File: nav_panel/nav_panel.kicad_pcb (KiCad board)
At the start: 2 copper layers, 45.7 x 22.6 mm, 12 parts, among them J1 Conn_01x04_Male, J2 Conn_01x04_Male, SW1 SW_Push, SW2 SW_Push

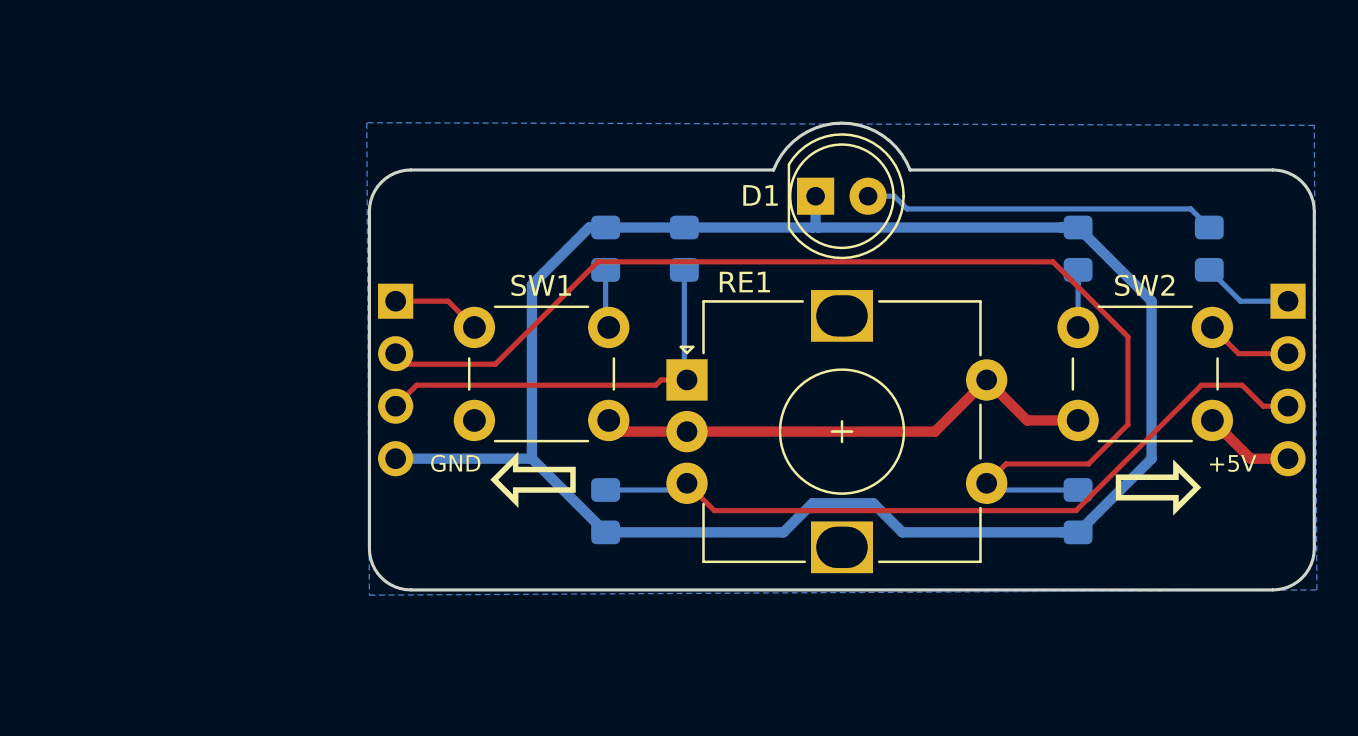
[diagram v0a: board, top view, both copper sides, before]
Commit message: Wide nav_panel version.
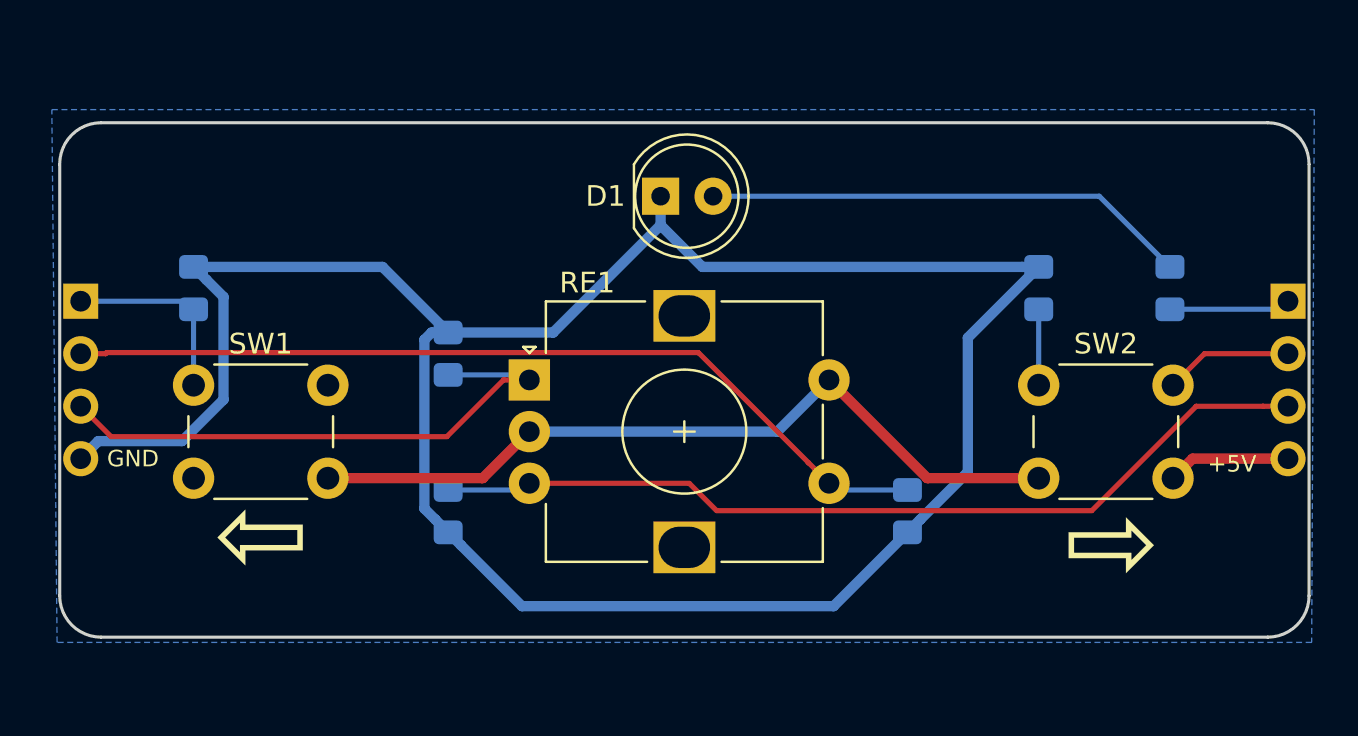
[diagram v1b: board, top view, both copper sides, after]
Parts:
- moved R1 20.0 mm to (117.2, 85.7)
- moved J1 15.2 mm to (111.8, 86.4)
- moved SW1 13.9 mm to (117.2, 90.4)
- moved R5 12.5 mm to (129.5, 88.9)
- moved R4 8.26 mm to (151.8, 96.5)
- moved RE1 7.63 mm to (133.5, 90.2)
- moved R3 7.62 mm to (129.5, 96.5)
- moved D1 7.50 mm to (139.8, 81.3)
- moved SW2 3.38 mm to (158.1, 90.4)
- moved R2 2.69 mm to (158.1, 85.7)
- moved R6 2.69 mm to (164.5, 85.7)
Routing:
- net GND: track 90.8 -> 113.5 mm
- net +5V: track 29.2 -> 44.3 mm
- net RE1: track 56.0 -> 42.8 mm
- net RE_A: track 20.0 -> 27.5 mm
- net RE_B: track 36.6 -> 43.4 mm
- net Net-(D1-Pad2): track 17.1 -> 23.5 mm
- net SW2: track 6.97 -> 9.87 mm
- net SW1: track 7.18 -> 9.30 mm
- net LED: track 4.44 -> 5.88 mm
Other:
- board size 45.7 x 22.6 mm -> 60.5 x 24.9 mm

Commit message: Printed and tested layout version.
USB still on upper board.
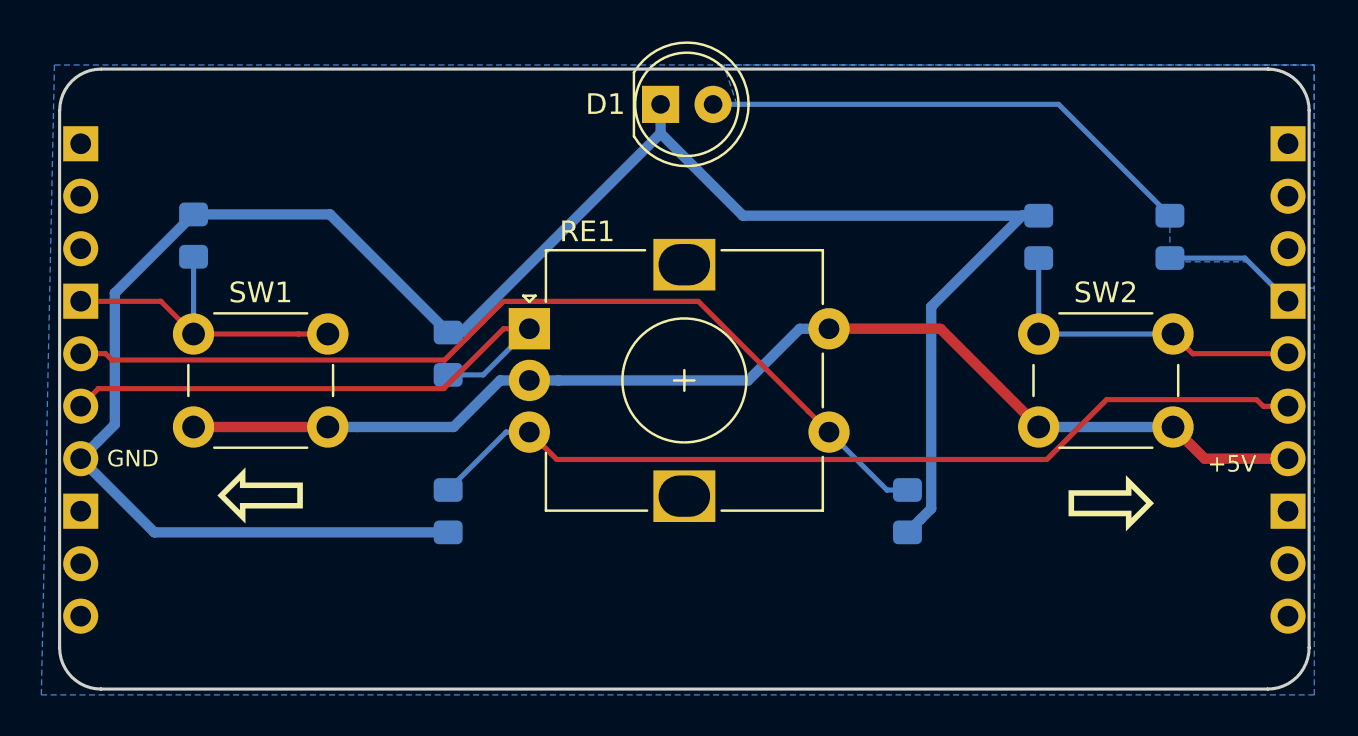
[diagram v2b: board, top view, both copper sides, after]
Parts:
- added REF**: PinHeader_1x03_P2.54mm_Vertical, Connector_PinHeader_2.54mm:PinHeader_1x03_P2.54mm_Vertical, B.Cu at (170.2, 78.7)
- added REF**: PinHeader_1x03_P2.54mm_Vertical, Connector_PinHeader_2.54mm:PinHeader_1x03_P2.54mm_Vertical, B.Cu at (170.2, 96.5)
- added REF**: PinHeader_1x03_P2.54mm_Vertical, Connector_PinHeader_2.54mm:PinHeader_1x03_P2.54mm_Vertical, B.Cu at (111.8, 96.5)
- added REF**: PinHeader_1x03_P2.54mm_Vertical, Connector_PinHeader_2.54mm:PinHeader_1x03_P2.54mm_Vertical, B.Cu at (111.8, 78.7)
- added REF**: KiCad-Logo2_5mm_SilkScreen, Symbol:KiCad-Logo2_5mm_SilkScreen, B.Cu at (130.2, 80.6)
- moved D1 4.45 mm to (139.8, 76.8)
- moved R1 2.54 mm to (117.2, 83.2)
- moved RE1 2.48 mm to (133.5, 87.7)
- moved SW1 2.48 mm to (117.2, 87.9)
- moved SW2 2.48 mm to (158.1, 87.9)
- moved R2 2.48 mm to (158.1, 83.2)
- moved R6 2.48 mm to (164.5, 83.2)
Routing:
- net +5V: track 44.3 -> 57.5 mm
- net GND: track 113.5 -> 102.1 mm
- net SW1: track 9.30 -> 16.4 mm
- net SW2: track 9.87 -> 16.1 mm
- net RE1: track 42.8 -> 45.1 mm
- net Net-(D1-Pad2): track 23.5 -> 24.3 mm
- net LED: track 5.88 -> 6.58 mm
- net RE_A: track 27.5 -> 28.1 mm
- added copper zone on B.Cu, net Net-(D1-Pad2)
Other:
- board size 60.5 x 24.9 mm -> 60.5 x 30 mm
- board text added: "2019.11.04"
- board text added: "https://github.com/mar0x/pq-4"
- board text added: "nav_panel"

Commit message: Production version 2019.11.19.
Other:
- board text added: "2019.11.18"
- board text added: "github.com/mar0x/pq-4"
- board text removed: "2019.11.04"
- board text removed: "https://github.com/mar0x/pq-4"
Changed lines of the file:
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@@
     (tags "resistor handsolder")
     (attr smd)
-    (fp_text reference R1 (at 1.397 1.778 90) (layer B.SilkS)
-      (effects (font (size 1 1) (thickness 0.15)) (justify mirror))
-    )
-    (fp_text value 10k (at -1.524 1.905 90) (layer B.SilkS)
+    (fp_text reference R1 (at 2.54 0.254 180) (layer B.SilkS)
+      (effects (font (size 1 1) (thickness 0.15)) (justify mirror))
+    )
+    (fp_text value 10k (at -2.54 0.254 180) (layer B.SilkS)
       (effects (font (size 1 1) (thickness 0.13)) (justify mirror))
     )
@@
     (tags "resistor handsolder")
     (attr smd)
-    (fp_text reference R2 (at 1.397 -1.651 90) (layer B.SilkS)
-      (effects (font (size 1 1) (thickness 0.15)) (justify mirror))
-    )
-    (fp_text value 10k (at -1.651 -1.651 90) (layer B.SilkS)
+    (fp_text reference R2 (at 2.6035 0 180) (layer B.SilkS)
+      (effects (font (size 1 1) (thickness 0.15)) (justify mirror))
+    )
+    (fp_text value 10k (at -2.4765 0 180) (layer B.SilkS)
       (effects (font (size 1 1) (thickness 0.13)) (justify mirror))
     )
@@
     (tags "resistor handsolder")
     (attr smd)
-    (fp_text reference R3 (at -1.397 1.65 270) (layer B.SilkS)
-      (effects (font (size 1 1) (thickness 0.15)) (justify mirror))
-    )
-    (fp_text value 10k (at 1.524 1.651 270) (layer B.SilkS)
+    (fp_text reference R3 (at -2.54 0) (layer B.SilkS)
+      (effects (font (size 1 1) (thickness 0.15)) (justify mirror))
+    )
+    (fp_text value 10k (at 2.54 0) (layer B.SilkS)
       (effects (font (size 1 1) (thickness 0.13)) (justify mirror))
     )
@@
     (tags "resistor handsolder")
     (attr smd)
-    (fp_text reference R4 (at -1.27 1.651 270) (layer B.SilkS)
-      (effects (font (size 1 1) (thickness 0.15)) (justify mirror))
-    )
-    (fp_text value 10k (at 1.524 1.651 270) (layer B.SilkS)
+    (fp_text reference R4 (at -2.54 0) (layer B.SilkS)
+      (effects (font (size 1 1) (thickness 0.15)) (justify mirror))
+    )
+    (fp_text value 10k (at 2.54 0) (layer B.SilkS)
       (effects (font (size 1 1) (thickness 0.13)) (justify mirror))
     )
@@
     (tags "resistor handsolder")
     (attr smd)
-    (fp_text reference R5 (at 1.397 -1.651 90) (layer B.SilkS)
-      (effects (font (size 1 1) (thickness 0.15)) (justify mirror))
-    )
-    (fp_text value 10k (at -1.524 -1.65 90) (layer B.SilkS)
+    (fp_text reference R5 (at 2.54 0 180) (layer B.SilkS)
+      (effects (font (size 1 1) (thickness 0.15)) (justify mirror))
+    )
+    (fp_text value 10k (at -2.54 0 180) (layer B.SilkS)
       (effects (font (size 1 1) (thickness 0.13)) (justify mirror))
     )
@@
     (tags "resistor handsolder")
     (attr smd)
-    (fp_text reference R6 (at -1.397 1.65 270) (layer B.SilkS)
-      (effects (font (size 1 1) (thickness 0.15)) (justify mirror))
-    )
-    (fp_text value 330 (at 1.778 1.651 270) (layer B.SilkS)
+    (fp_text reference R6 (at -2.6035 0) (layer B.SilkS)
+      (effects (font (size 1 1) (thickness 0.15)) (justify mirror))
+    )
+    (fp_text value 330 (at 2.4765 0) (layer B.SilkS)
       (effects (font (size 1 1) (thickness 0.13)) (justify mirror))
     )
@@
       (xy -2.9464 2.607733) (xy -2.9464 2.510946)) (layer B.SilkS) (width 0.01))
   )
-  (gr_text https://github.com/mar0x/pq-4 (at 156.845 103.505) (layer B.SilkS)
-    (effects (font (size 0.8 0.7) (thickness 0.15)) (justify mirror))
+  (gr_text github.com/mar0x/pq-4 (at 155.575 102.87) (layer B.SilkS)
+    (effects (font (size 0.9 1) (thickness 0.15)) (justify mirror))
   )
   (dimension 4.572 (width 0.3) (layer F.Fab)
@@
   )
   (gr_line (start 108.585 90.17) (end 173.228 90.17) (layer F.Fab) (width 0.05))
-  (gr_text 2019.11.04 (at 121.92 102.87) (layer B.SilkS)
-    (effects (font (size 0.6 0.6) (thickness 0.1)) (justify mirror))
+  (gr_text 2019.11.18 (at 120.65 102.87) (layer B.SilkS)
+    (effects (font (size 0.9 0.9) (thickness 0.2)) (justify mirror))
   )
   (gr_text nav_panel (at 127.635 100.965) (layer B.SilkS)
-    (effects (font (size 1.5 1.5) (thickness 0.3)) (justify mirror))
+    (effects (font (size 2 2) (thickness 0.3)) (justify mirror))
   )
   (gr_line (start 120.47 82.296) (end 120.47 97.8154) (layer F.Fab) (width 0.08))
